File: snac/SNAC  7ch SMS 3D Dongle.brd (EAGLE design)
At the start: 37.2 x 21.9 mm, 11 parts, among them IC1 4030D, K2 692112030100, Q9 BC849SMD, X2 STEREOJACK

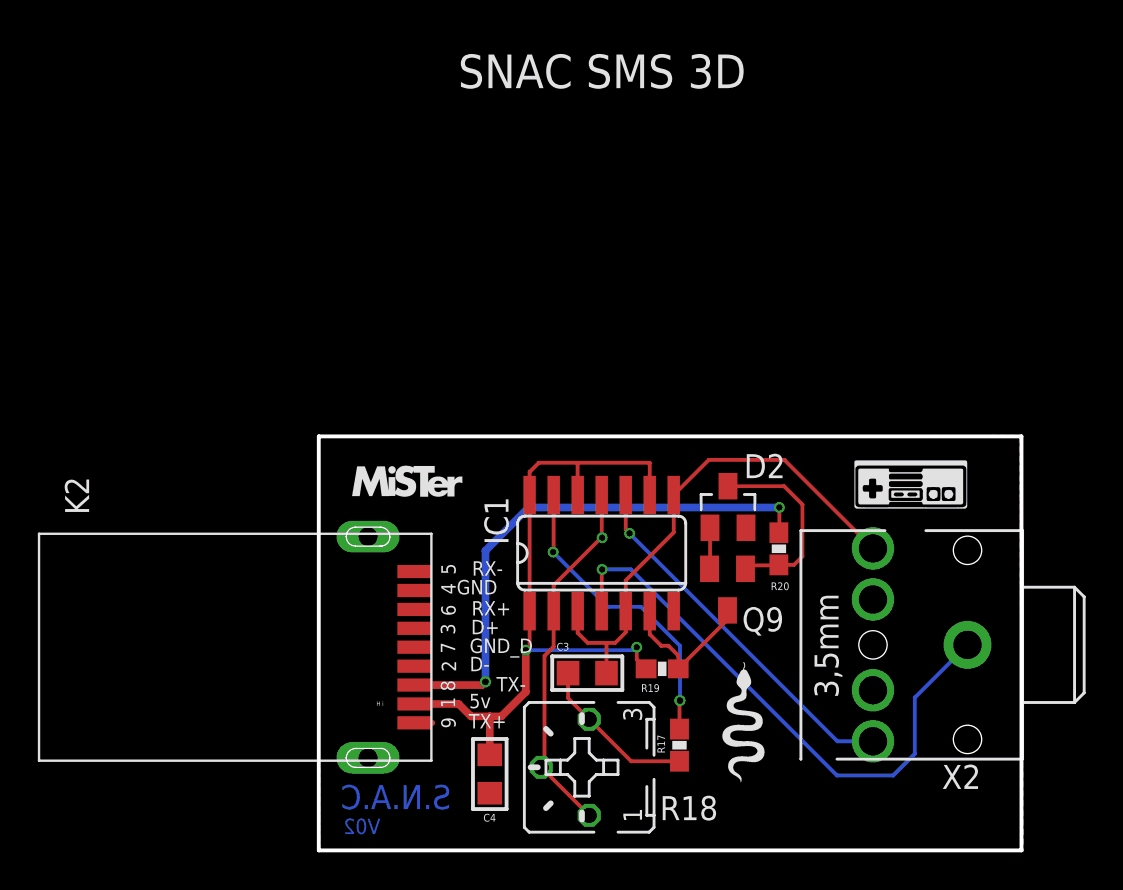
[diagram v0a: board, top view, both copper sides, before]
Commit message: Changed SMS 3D Dongle back to using LV7 on USER IO
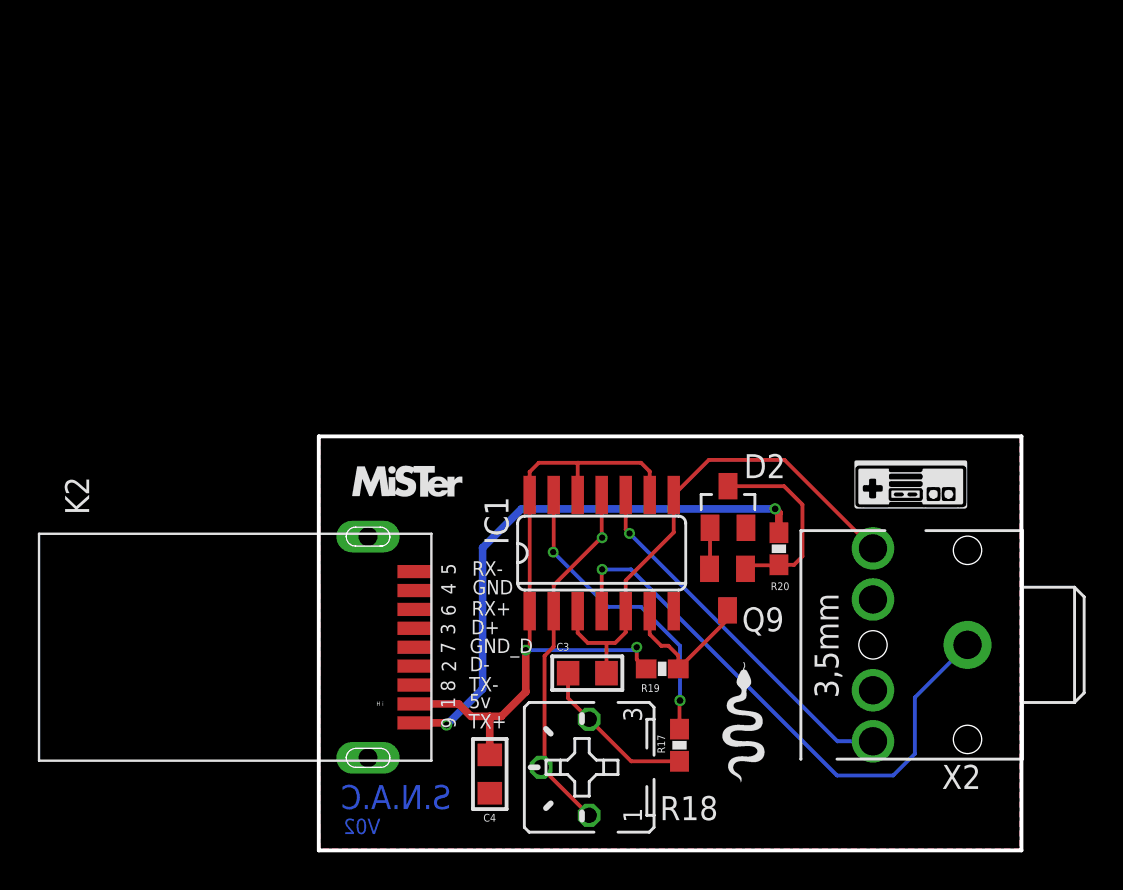
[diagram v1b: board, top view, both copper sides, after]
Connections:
- net LV1: no longer R20.1
- net LV7: now also R20.1
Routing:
- net LV7: track 0.95 -> 29.6 mm, vias 0 -> 2
- net LV1: track 28.6 -> 0.00 mm, vias 2 -> 0
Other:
- board text removed: "SNAC SMS 3D"
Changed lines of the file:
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@@
 <text x="8.128" y="14.4526" size="0.762" layer="21" font="vector" ratio="15">RX-</text>
 <text x="8.1026" y="12.3444" size="0.762" layer="21" font="vector" ratio="15">RX+</text>
-<text x="9.4234" y="8.3312" size="0.762" layer="21" font="vector" ratio="15">TX-</text>
+<text x="7.9756" y="8.3312" size="0.762" layer="21" font="vector" ratio="15">TX-</text>
 <text x="7.9756" y="7.4422" size="0.762" layer="21" font="vector" ratio="15">5v</text>
 <text x="8.001" y="10.3632" size="0.762" layer="21" font="vector" ratio="15">GND_D</text>
 <text x="7.9502" y="6.3754" size="0.762" layer="21" font="vector" ratio="15">TX+</text>
-<text x="7.3152" y="13.462" size="0.762" layer="21" font="vector" ratio="15">GND</text>
+<text x="8.1534" y="13.462" size="0.762" layer="21" font="vector" ratio="15">GND</text>
 <rectangle x1="28.464509375" y1="17.99716875" x2="34.202371875" y2="18.0047875" layer="21"/>
 <rectangle x1="28.43403125" y1="18.0047875" x2="34.23285" y2="18.01240625" layer="21"/>
@@
 <rectangle x1="22.49805" y1="9.89965" x2="22.51075" y2="9.91235" layer="22"/>
 <rectangle x1="22.48535" y1="9.91235" x2="22.49805" y2="9.92505" layer="22"/>
-<text x="7.3914" y="40.2336" size="1.778" layer="21">SNAC SMS 3D</text>
 </plain>
 <attributes>
@@
 <signals>
 <signal name="GND">
-<polygon width="0.254" layer="1">
-<vertex x="0" y="21.8186"/>
-<vertex x="37.084" y="21.7932"/>
-<vertex x="37.211" y="-0.127"/>
-<vertex x="0.0254" y="-0.0762"/>
-</polygon>
-<polygon width="0.254" layer="16">
-<vertex x="0" y="21.7932"/>
-<vertex x="37.1348" y="21.8694"/>
-<vertex x="37.2872" y="-0.127"/>
-<vertex x="0.0762" y="-0.0762"/>
-</polygon>
 <contactref element="K2" pad="4"/>
 <contactref element="IC1" pad="7"/>
@@
 <wire x1="20.6908" y1="14.816" x2="20.7162" y2="14.9938" width="0.2032" layer="1"/>
 <wire x1="20.7162" y1="14.9938" x2="20.7162" y2="16.9848" width="0.2032" layer="1"/>
+<polygon width="0.1524" layer="16">
+<vertex x="0.0762" y="21.7932"/>
+<vertex x="37.1094" y="21.7932"/>
+<vertex x="37.1094" y="0"/>
+<vertex x="0.0762" y="0"/>
+</polygon>
+<polygon width="0.1524" layer="1">
+<vertex x="0.0762" y="21.7932"/>
+<vertex x="37.1094" y="21.7932"/>
+<vertex x="37.1094" y="0"/>
+<vertex x="0.0762" y="0"/>
+</polygon>
 </signal>
 <signal name="HV">
@@
 <wire x1="11.176" y1="19.939" x2="11.6586" y2="20.4216" width="0.2032" layer="1"/>
 <wire x1="11.6586" y1="20.4216" x2="13.716" y2="20.4216" width="0.2032" layer="1"/>
-<wire x1="13.716" y1="20.4216" x2="17.526" y2="20.4216" width="0.2032" layer="1"/>
 <wire x1="13.716" y1="18.7198" x2="13.716" y2="20.4216" width="0.2032" layer="1"/>
 <via x="10.9728" y="10.5156" extent="1-16" drill="0.3302"/>
@@
 <wire x1="16.8402" y1="10.668" x2="16.8402" y2="10.0212" width="0.2032" layer="1"/>
 <wire x1="16.8402" y1="10.0212" x2="17.3364" y2="9.525" width="0.2032" layer="1"/>
-<wire x1="17.526" y1="18.7198" x2="17.526" y2="20.4216" width="0.2032" layer="1"/>
 <wire x1="5.08" y1="7.668" x2="7.4196" y2="7.668" width="0.4064" layer="1"/>
 <wire x1="7.4196" y1="7.668" x2="8.0772" y2="7.0104" width="0.4064" layer="1"/>
@@
 <wire x1="9.6774" y1="7.0104" x2="10.9728" y2="8.3058" width="0.4064" layer="1"/>
 <wire x1="9.0678" y1="4.9784" x2="9.0678" y2="7.0104" width="0.4064" layer="1"/>
+<wire x1="13.716" y1="20.4216" x2="17.0688" y2="20.4216" width="0.2032" layer="1"/>
+<wire x1="17.526" y1="19.9644" x2="17.526" y2="18.7198" width="0.2032" layer="1"/>
+<wire x1="17.0688" y1="20.4216" x2="17.526" y2="19.9644" width="0.2032" layer="1"/>
 </signal>
 <signal name="LV2">
@@
 <signal name="LV1">
 <contactref element="K2" pad="8"/>
-<contactref element="R20" pad="1"/>
-<via x="24.384" y="18.0594" extent="1-16" drill="0.3302"/>
-<wire x1="24.3586" y1="16.725" x2="24.384" y2="16.7504" width="0.2032" layer="1"/>
-<wire x1="24.384" y1="16.7504" x2="24.384" y2="18.0594" width="0.2032" layer="1"/>
-<wire x1="5.08" y1="8.668" x2="8.668" y2="8.668" width="0.4064" layer="1"/>
-<wire x1="8.668" y1="8.668" x2="8.8392" y2="8.8392" width="0.4064" layer="1"/>
-<via x="8.8392" y="8.8392" extent="1-16" drill="0.35"/>
-<wire x1="8.8392" y1="8.8392" x2="8.8392" y2="15.7734" width="0.4064" layer="16"/>
-<wire x1="8.8392" y1="15.7734" x2="11.1252" y2="18.0594" width="0.4064" layer="16"/>
-<wire x1="11.1252" y1="18.0594" x2="24.384" y2="18.0594" width="0.4064" layer="16"/>
 </signal>
 <signal name="LV4">
@@
 <signal name="LV7">
 <contactref element="K2" pad="9"/>
-<wire x1="5.08" y1="6.668" x2="6.032" y2="6.668" width="0.3048" layer="1"/>
+<contactref element="R20" pad="1"/>
+<wire x1="24.3586" y1="16.725" x2="24.3586" y2="17.78" width="0.4064" layer="1"/>
+<wire x1="24.3586" y1="17.78" x2="24.1554" y2="17.9832" width="0.4064" layer="1"/>
+<via x="24.1554" y="17.9832" extent="1-16" drill="0.35"/>
+<wire x1="24.1554" y1="17.9832" x2="10.7442" y2="17.9832" width="0.4064" layer="16"/>
+<wire x1="10.7442" y1="17.9832" x2="8.6868" y2="15.9258" width="0.4064" layer="16"/>
+<wire x1="8.6868" y1="15.9258" x2="8.6868" y2="8.4582" width="0.4064" layer="16"/>
+<wire x1="8.6868" y1="8.4582" x2="6.7818" y2="6.5532" width="0.4064" layer="16"/>
+<via x="6.7818" y="6.5532" extent="1-16" drill="0.35"/>
+<wire x1="6.7818" y1="6.5532" x2="6.668" y2="6.668" width="0.4064" layer="1"/>
+<wire x1="6.668" y1="6.668" x2="5.08" y2="6.668" width="0.4064" layer="1"/>
 </signal>
 <signal name="N$1">

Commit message: SMS 3D and SNES SNAC JST updates
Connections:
- net N$6 renamed TIP
- net N$7 renamed SLEEVE
- net N$8 renamed RING
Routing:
- net HV: track 37.6 -> 35.6 mm
- net LV7: track 29.6 -> 31.3 mm
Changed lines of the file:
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@@
 <setting verticaltext="up"/>
 </settings>
-<grid distance="3" unitdist="mil" unit="mil" style="lines" multiple="1" display="no" altdistance="0.001" altunitdist="inch" altunit="inch"/>
+<grid distance="3" unitdist="mil" unit="mm" style="lines" multiple="1" display="no" altdistance="0.001" altunitdist="inch" altunit="inch"/>
 <layers>
 <layer number="1" name="Top" color="4" fill="1" visible="yes" active="yes"/>
@@
 <layer number="44" name="Drills" color="7" fill="1" visible="no" active="yes"/>
 <layer number="45" name="Holes" color="7" fill="1" visible="yes" active="yes"/>
-<layer number="46" name="Milling" color="3" fill="1" visible="no" active="yes"/>
+<layer number="46" name="Milling" color="3" fill="1" visible="yes" active="yes"/>
 <layer number="47" name="Measures" color="7" fill="1" visible="no" active="yes"/>
 <layer number="48" name="Document" color="7" fill="1" visible="no" active="yes"/>
@@
 <contactref element="IC1" pad="7"/>
 <contactref element="Q9" pad="E"/>
-<contactref element="C4" pad="2"/>
 <contactref element="D2" pad="1"/>
 <wire x1="20.6908" y1="14.4678" x2="20.6908" y2="14.816" width="0.2032" layer="1"/>
@@
 <vertex x="0.0762" y="0"/>
 </polygon>
+<contactref element="C4" pad="2"/>
 </signal>
 <signal name="HV">
@@
 <contactref element="R19" pad="1"/>
 <contactref element="IC1" pad="12"/>
-<contactref element="C4" pad="1"/>
 <contactref element="IC1" pad="14"/>
 <wire x1="11.0744" y1="12.6746" x2="11.176" y2="12.573" width="0.2032" layer="1"/>
@@
 <wire x1="10.9728" y1="8.3058" x2="10.9728" y2="10.5156" width="0.4064" layer="1"/>
 <wire x1="9.6774" y1="7.0104" x2="10.9728" y2="8.3058" width="0.4064" layer="1"/>
-<wire x1="9.0678" y1="4.9784" x2="9.0678" y2="7.0104" width="0.4064" layer="1"/>
 <wire x1="13.716" y1="20.4216" x2="17.0688" y2="20.4216" width="0.2032" layer="1"/>
 <wire x1="17.526" y1="19.9644" x2="17.526" y2="18.7198" width="0.2032" layer="1"/>
 <wire x1="17.0688" y1="20.4216" x2="17.526" y2="19.9644" width="0.2032" layer="1"/>
+<contactref element="C4" pad="1"/>
+<wire x1="9.0678" y1="4.9784" x2="9.0678" y2="7.0104" width="0" layer="19" extent="1-1"/>
 </signal>
 <signal name="LV2">
@@
 <wire x1="24.1554" y1="17.9832" x2="10.7442" y2="17.9832" width="0.4064" layer="16"/>
 <wire x1="10.7442" y1="17.9832" x2="8.6868" y2="15.9258" width="0.4064" layer="16"/>
-<wire x1="8.6868" y1="15.9258" x2="8.6868" y2="8.4582" width="0.4064" layer="16"/>
-<wire x1="8.6868" y1="8.4582" x2="6.7818" y2="6.5532" width="0.4064" layer="16"/>
-<via x="6.7818" y="6.5532" extent="1-16" drill="0.35"/>
-<wire x1="6.7818" y1="6.5532" x2="6.668" y2="6.668" width="0.4064" layer="1"/>
-<wire x1="6.668" y1="6.668" x2="5.08" y2="6.668" width="0.4064" layer="1"/>
+<via x="6.7056" y="5.5626" extent="1-16" drill="0.35"/>
+<wire x1="8.6868" y1="7.5438" x2="6.7056" y2="5.5626" width="0.4064" layer="16"/>
+<wire x1="8.6868" y1="15.9258" x2="8.6868" y2="7.5438" width="0.4064" layer="16"/>
+<wire x1="5.08" y1="6.668" x2="6.286" y2="6.668" width="0.4064" layer="1"/>
+<wire x1="6.7056" y1="6.2484" x2="6.7056" y2="5.5626" width="0.4064" layer="1"/>
+<wire x1="6.286" y1="6.668" x2="6.7056" y2="6.2484" width="0.4064" layer="1"/>
 </signal>
 <signal name="N$1">
@@
 <wire x1="11.9634" y1="4.4958" x2="11.7856" y2="4.318" width="0.2032" layer="1"/>
 </signal>
-<signal name="N$6">
+<signal name="TIP">
 <contactref element="IC1" pad="3"/>
 <contactref element="IC1" pad="8"/>
@@
 <wire x1="24.6526" y1="20.574" x2="29.3332" y2="15.8934" width="0.2032" layer="1"/>
 </signal>
-<signal name="N$7">
+<signal name="SLEEVE">
 <contactref element="IC1" pad="4"/>
 <contactref element="X2" pad="1"/>
@@
 <wire x1="27.432" y1="3.8862" x2="16.5354" y2="14.7828" width="0.2032" layer="16"/>
 </signal>
-<signal name="N$8">
+<signal name="RING">
 <contactref element="IC1" pad="10"/>
 <contactref element="X2" pad="2"/>

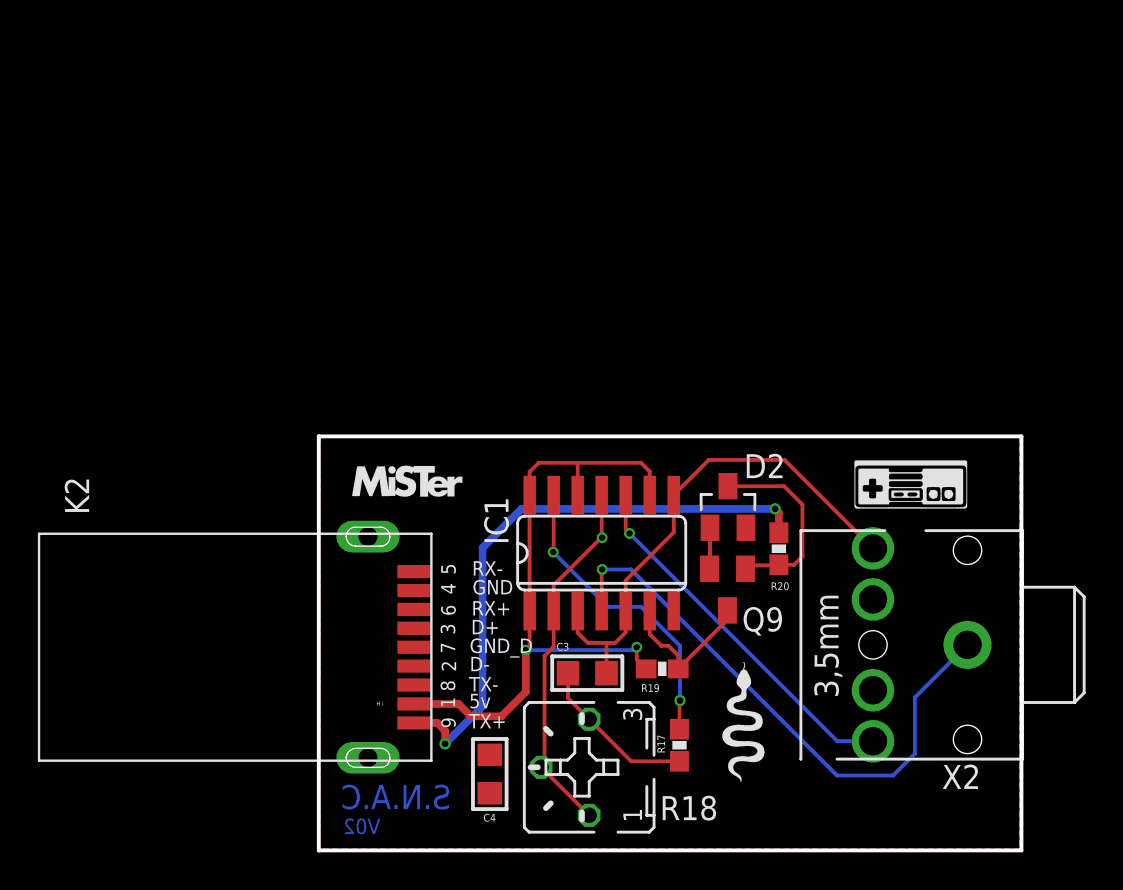
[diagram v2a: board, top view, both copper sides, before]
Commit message: changed from LV7 to LV5 pin, for the 3D Glasses boards
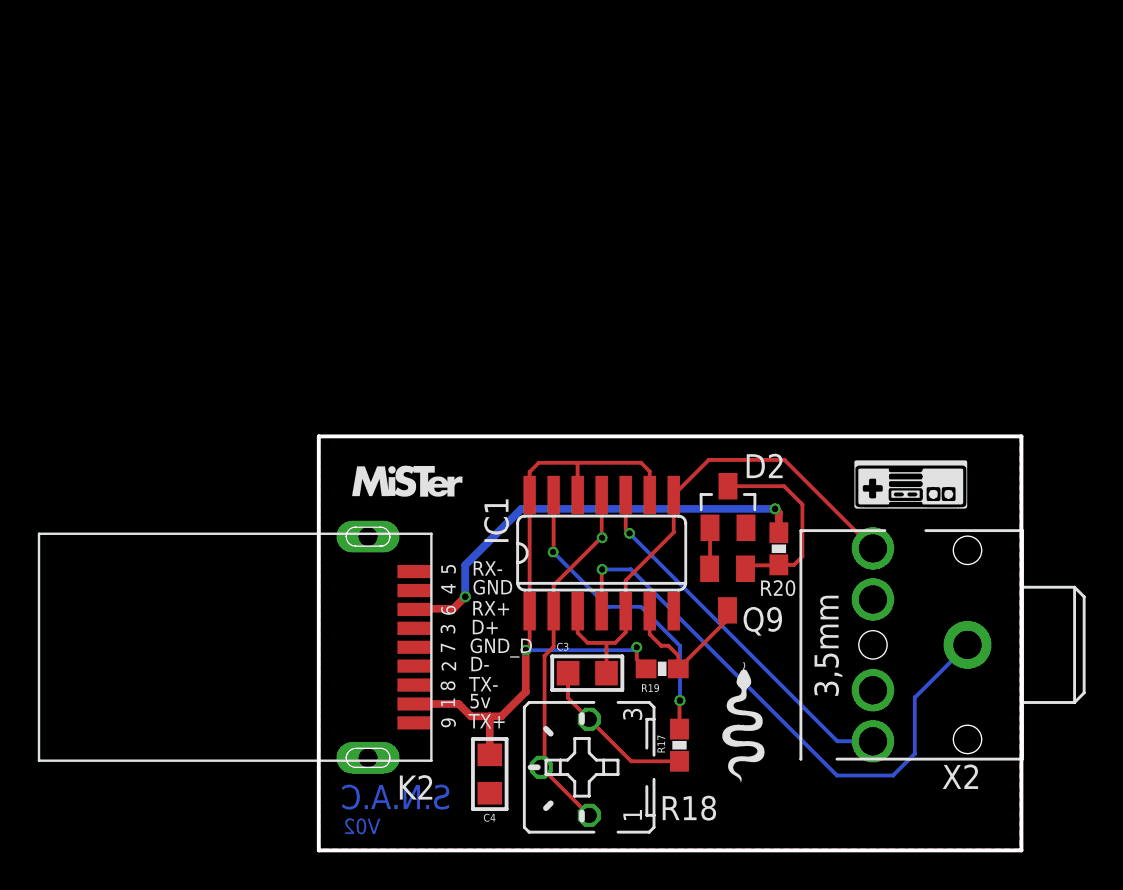
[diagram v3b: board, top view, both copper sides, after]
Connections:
- net LV5: now also R20.1
- net LV7: no longer R20.1
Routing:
- net LV7: track 31.3 -> 0.00 mm, vias 2 -> 0
- net LV5: track 0.03 -> 23.6 mm, vias 0 -> 2
- net HV: track 35.6 -> 37.6 mm
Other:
- board text removed: "H i"
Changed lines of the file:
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@@
 <rectangle x1="22.49805" y1="9.87425" x2="22.52345" y2="9.88695" layer="21"/>
 <text x="1.7526" y="12.9032" size="0.762" layer="22" font="vector" ratio="15" rot="MR270">MISTER</text>
-<text x="3.0734" y="7.5692" size="0.2286" layer="21" ratio="15">H i</text>
 <rectangle x1="22.30755" y1="3.48615" x2="22.32025" y2="3.49885" layer="22"/>
 <rectangle x1="22.30755" y1="3.49885" x2="22.33295" y2="3.51155" layer="22"/>
@@
 </autorouter>
 <elements>
-<element name="K2" library="Wuerth_Elektronik_eiCan_Communication_Connectors_STENCIL" package="692112030100" value="692112030100" x="5.08" y="10.668" rot="R90"/>
+<element name="K2" library="Wuerth_Elektronik_eiCan_Communication_Connectors_STENCIL" package="692112030100" value="692112030100" x="5.08" y="10.668" smashed="yes" rot="R90">
+<attribute name="NAME" x="6.1826" y="3.882" size="1.27" layer="25" rot="R180"/>
+<attribute name="VALUE" x="-9.92" y="17.668" size="1.27" layer="27" rot="R90"/>
+</element>
 <element name="IC1" library="40xx" package="SO14" value="4030D" x="14.986" y="15.6464" smashed="yes">
 <attribute name="NAME" x="10.0584" y="16.0782" size="1.27" layer="25" ratio="10" rot="R90"/>
@@
 </element>
 <element name="R20" library="SparkFun" package="0603-RES" value="10K" x="24.3586" y="15.875" smashed="yes" rot="R270">
-<attribute name="NAME" x="23.9268" y="13.6906" size="0.4064" layer="25" font="vector"/>
+<attribute name="NAME" x="23.3172" y="13.3858" size="0.8128" layer="25"/>
 <attribute name="VALUE" x="23.2156" y="16.891" size="0.4064" layer="27" font="vector" rot="R270"/>
 </element>
@@
 <wire x1="17.0688" y1="20.4216" x2="17.526" y2="19.9644" width="0.2032" layer="1"/>
 <contactref element="C4" pad="1"/>
-<wire x1="9.0678" y1="4.9784" x2="9.0678" y2="7.0104" width="0" layer="19" extent="1-1"/>
+<wire x1="9.0678" y1="4.9784" x2="9.0678" y2="7.0104" width="0.4064" layer="1"/>
 </signal>
 <signal name="LV2">
@@
 <contactref element="K2" pad="6"/>
 <wire x1="5.08" y1="12.7" x2="5.08" y2="12.668" width="0.1778" layer="1"/>
+<contactref element="R20" pad="1"/>
+<wire x1="24.3586" y1="16.725" x2="24.3586" y2="17.78" width="0.4064" layer="1"/>
+<wire x1="24.3586" y1="17.78" x2="24.1554" y2="17.9832" width="0.4064" layer="1"/>
+<via x="24.1554" y="17.9832" extent="1-16" drill="0.35"/>
+<wire x1="24.1554" y1="17.9832" x2="10.7442" y2="17.9832" width="0.4064" layer="16"/>
+<wire x1="7.7724" y1="15.0114" x2="7.7724" y2="13.335" width="0.4064" layer="16"/>
+<via x="7.7724" y="13.335" extent="1-16" drill="0.35"/>
+<wire x1="7.7724" y1="13.335" x2="7.1374" y2="12.7" width="0.4064" layer="1"/>
+<wire x1="7.1374" y1="12.7" x2="5.08" y2="12.7" width="0.4064" layer="1"/>
+<wire x1="10.7442" y1="17.9832" x2="7.7724" y2="15.0114" width="0.4064" layer="16"/>
 </signal>
 <signal name="LV6">
@@
 <signal name="LV7">
 <contactref element="K2" pad="9"/>
-<contactref element="R20" pad="1"/>
-<wire x1="24.3586" y1="16.725" x2="24.3586" y2="17.78" width="0.4064" layer="1"/>
-<wire x1="24.3586" y1="17.78" x2="24.1554" y2="17.9832" width="0.4064" layer="1"/>
-<via x="24.1554" y="17.9832" extent="1-16" drill="0.35"/>
-<wire x1="24.1554" y1="17.9832" x2="10.7442" y2="17.9832" width="0.4064" layer="16"/>
-<wire x1="10.7442" y1="17.9832" x2="8.6868" y2="15.9258" width="0.4064" layer="16"/>
-<via x="6.7056" y="5.5626" extent="1-16" drill="0.35"/>
-<wire x1="8.6868" y1="7.5438" x2="6.7056" y2="5.5626" width="0.4064" layer="16"/>
-<wire x1="8.6868" y1="15.9258" x2="8.6868" y2="7.5438" width="0.4064" layer="16"/>
-<wire x1="5.08" y1="6.668" x2="6.286" y2="6.668" width="0.4064" layer="1"/>
-<wire x1="6.7056" y1="6.2484" x2="6.7056" y2="5.5626" width="0.4064" layer="1"/>
-<wire x1="6.286" y1="6.668" x2="6.7056" y2="6.2484" width="0.4064" layer="1"/>
 </signal>
 <signal name="N$1">
